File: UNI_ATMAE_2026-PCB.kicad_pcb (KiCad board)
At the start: 2 copper layers, 100 x 100 mm, 5 parts, among them J1 Power In, J2 Motor Driver, J3 Out 1, U1 ESP32, U2 Buck Converter

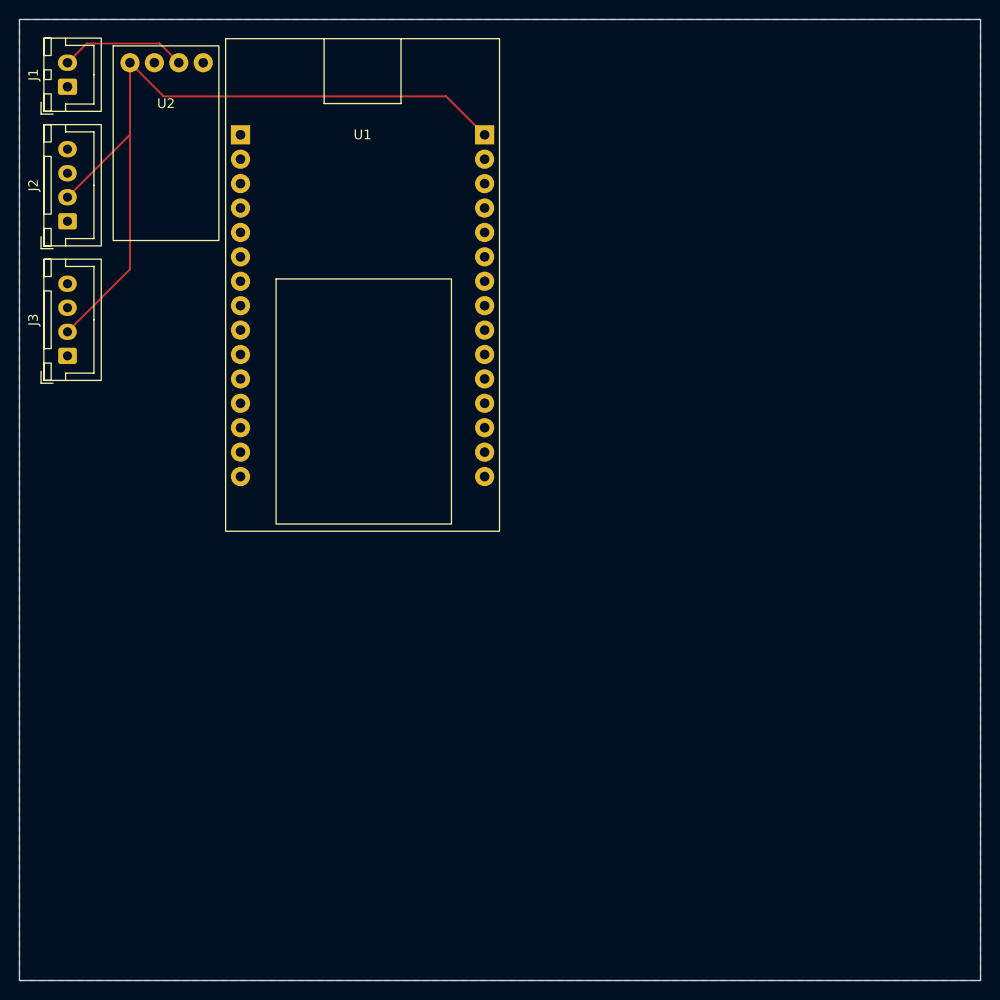
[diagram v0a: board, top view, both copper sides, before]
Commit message: Oct-15-26
Added Logic Level shifter symbol/footprint
Updated labels on project schematics to not move when added to project
Basic test PCB design
Added README file
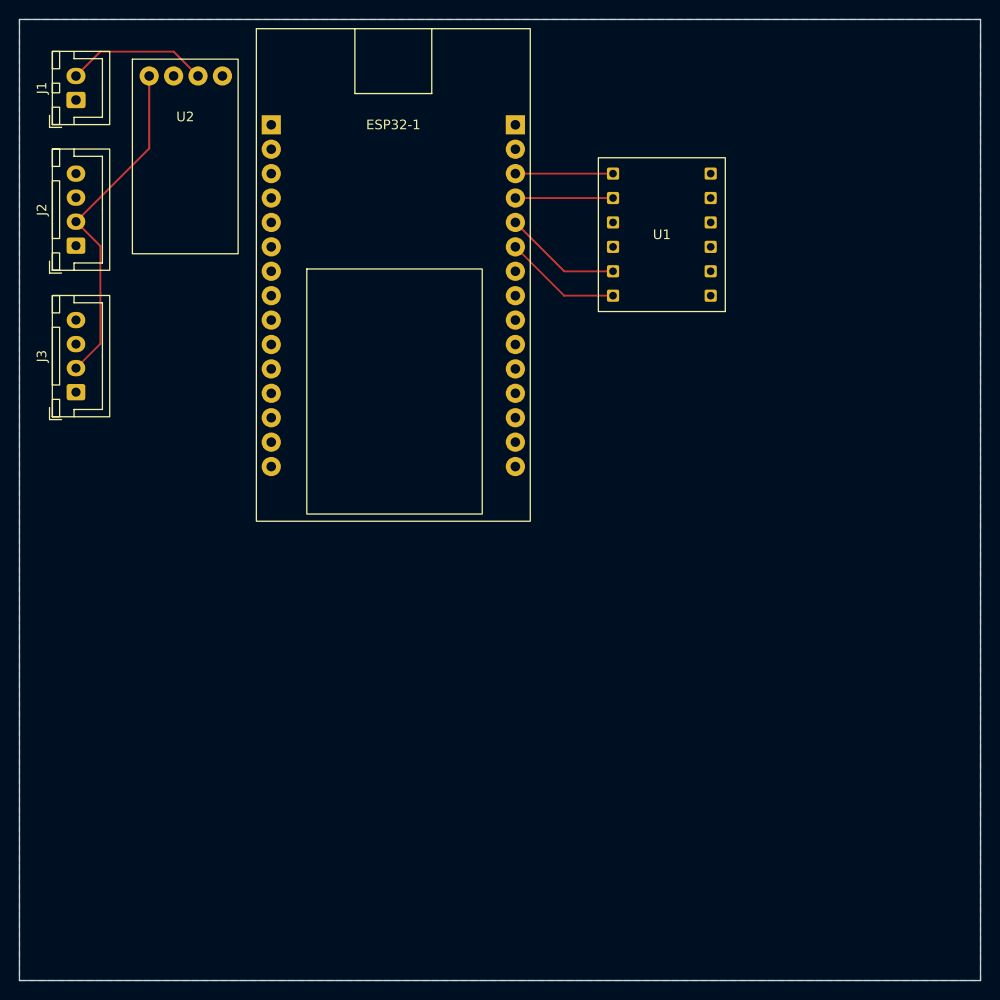
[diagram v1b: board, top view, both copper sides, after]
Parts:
- added ESP32-1: ESP32, Project Footprints:ESP32_DevBoard, F.Cu at (74.7, 51.0)
- U1: value ESP32 -> LVL Shifter; footprint Project Footprints:ESP32_DevBoard -> Project Footprints:Logic Level Shifter-4Ch
- U2: value Buck Converter -> Buck Conv.
- moved U1 57.1 mm to (121.9, 78.7), turned to 180 degrees
- moved J3 3.88 mm to (55.9, 88.8)
- moved J2 2.69 mm to (55.9, 73.5)
- moved U2 2.43 mm to (61.8, 54.1)
- moved J1 1.64 mm to (55.9, 58.4)
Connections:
- U1 pad 11: unconnected-(U1-D21-Pad11) -> /D12
- U1 pad 12: unconnected-(U1-RX2-Pad12) -> /D13
- U1 pad 2: GND -> unconnected-(U1-HV2-Pad2)
- U1 pad 7: unconnected-(U1-TX0-Pad7) -> /D27
- U1 pad 8: unconnected-(U1-D5-Pad8) -> /D14
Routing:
- net Net-(J2-Pin_2): track 87.4 -> 35.7 mm
- net /D27: track 0.00 -> 12.3 mm
- net /D14: track 0.00 -> 12.3 mm
- net /D13: track 0.00 -> 10.2 mm
- net /D12: track 0.00 -> 10.2 mm
- net Net-(J1-Pin_2): track 13.2 -> 14.8 mm

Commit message: Oct-15-26
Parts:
- added J4: Out 1, Connector_JST:JST_XH_B4B-XH-A_1x04_P2.50mm_Vertical, F.Cu at (127.0, 54.0)
- moved J3 74.1 mm to (127.0, 67.9), turned to -90 degrees
- moved U1 14.1 mm to (117.5, 65.4)
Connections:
- ESP32-1 pad 12: unconnected-(ESP32-1-D16/RX2-Pad12) -> Net-(ESP32-1-D16/RX2)
- ESP32-1 pad 13: unconnected-(ESP32-1-D17/TX2-Pad13) -> Net-(ESP32-1-D17/TX2)
- ESP32-1 pad 16: unconnected-(ESP32-1-VIN-Pad16) -> /5V
- J1 pad 2: Net-(J1-Pin_2) -> /5V
- J2 pad 2: Net-(J2-Pin_2) -> /5V
- J2 pad 3: unconnected-(J2-Pin_3-Pad3) -> Net-(ESP32-1-D17/TX2)
- J2 pad 4: unconnected-(J2-Pin_4-Pad4) -> Net-(ESP32-1-D16/RX2)
- J3 pad 2: Net-(J2-Pin_2) -> /5V
- J3 pad 3: unconnected-(J3-Pin_3-Pad3) -> Net-(J3-Pin_3)
- J3 pad 4: unconnected-(J3-Pin_4-Pad4) -> Net-(J3-Pin_4)
- U1 pad 1: unconnected-(U1-HV1-Pad1) -> Net-(J3-Pin_4)
- U1 pad 10: unconnected-(U1-GND-Pad10) -> GND
- U1 pad 2: unconnected-(U1-HV2-Pad2) -> Net-(J3-Pin_3)
- U1 pad 3: unconnected-(U1-HV-Pad3) -> /5V
- U1 pad 4: unconnected-(U1-GND-Pad4) -> GND
- U1 pad 5: unconnected-(U1-HV3-Pad5) -> Net-(J4-Pin_4)
- U1 pad 6: unconnected-(U1-HV4-Pad6) -> Net-(J4-Pin_3)
- U1 pad 9: unconnected-(U1-LV-Pad9) -> /3.3V
- U2 pad 1: Net-(J2-Pin_2) -> /3.3V
- U2 pad 3: Net-(J1-Pin_2) -> /5V
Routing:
- net /5V: track 0.00 -> 109.7 mm
- net /3.3V: track 0.00 -> 45.7 mm
- net Net-(J2-Pin_2): track 35.7 -> 0.00 mm
- net Net-(ESP32-1-D17/TX2): track 0.00 -> 31.3 mm
- net Net-(ESP32-1-D16/RX2): track 0.00 -> 31.3 mm
- net Net-(J1-Pin_2): track 14.8 -> 0.00 mm
- net Net-(J3-Pin_3): track 0.00 -> 14.0 mm
- net Net-(J3-Pin_4): track 0.00 -> 14.0 mm
- net Net-(J4-Pin_3): track 0.00 -> 12.1 mm
- net Net-(J4-Pin_4): track 0.00 -> 12.1 mm
- net /D13: track 10.2 -> 16.8 mm
- net /D12: track 10.2 -> 15.7 mm
- net /D27: track 12.3 -> 10.6 mm
- net /D14: track 12.3 -> 10.6 mm

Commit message: Oct-15-26
Connected generic JST-XH connectors for 8 I/O pins through level shifters
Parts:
- added J5: Out 3, Connector_JST:JST_XH_B4B-XH-A_1x04_P2.50mm_Vertical, F.Cu at (127.0, 95.9)
- added J6: Out 4, Connector_JST:JST_XH_B4B-XH-A_1x04_P2.50mm_Vertical, F.Cu at (127.0, 81.9)
- added U3: LVL Shifter, Project Footprints:Logic Level Shifter-4Ch, F.Cu at (117.5, 83.2)
- J4: value Out 1 -> Out 2
- renumbered U2 to U1, U1 to U2
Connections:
- ESP32-1 pad 1: unconnected-(ESP32-1-3V3-Pad1) -> /3.3V
- ESP32-1 pad 25: unconnected-(ESP32-1-D32-Pad25) -> /D32
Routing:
- net /5V: track 109.7 -> 170.8 mm
- net Net-(J5-Pin_3): track 0.00 -> 24.2 mm
- net Net-(J5-Pin_4): track 0.00 -> 24.1 mm
- net /3.3V: track 45.7 -> 66.5 mm
- net Net-(J6-Pin_3): track 0.00 -> 20.4 mm
- net Net-(J6-Pin_4): track 0.00 -> 20.3 mm
- net /D26: track 0.00 -> 8.08 mm
- net /D25: track 0.00 -> 8.08 mm
- net /D33: track 0.00 -> 5.98 mm
- net /D32: track 0.00 -> 5.98 mm
